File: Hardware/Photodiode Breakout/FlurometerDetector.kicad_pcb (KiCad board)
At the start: 2 copper layers, 25.4 x 25.4 mm, 6 parts, among them U1 OPA333xxDBV

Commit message: Breakout rearranging, LED wiring
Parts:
- moved C1 8.35 mm to (142.0, 70.4)
- moved U1 8.35 mm to (138.2, 67.8)
- moved C2 8.35 mm to (141.9, 68.5)
- moved D1 8.35 mm to (133.5, 68.9)
- moved R1 8.35 mm to (141.9, 66.5)
- moved Conn1 8.35 mm to (129.9, 62.1)
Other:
- board outline removed
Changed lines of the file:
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@@
   (net 4 "GND")
   (footprint "MRDT_Connectors:MOLEX_SL_03_Horizontal" (layer "F.Cu")
-    (at 135.89 67.945)
+    (at 129.921 62.103)
     (property "Sheetfile" "FlurometerDetector.kicad_sch")
     (property "Sheetname" "")
@@
   )
   (footprint "Package_TO_SOT_THT:TO-18-2" (layer "F.Cu")
-    (at 139.515276 74.745276 180)
+    (at 133.546276 68.903276 180)
     (descr "TO-18-2")
     (tags "TO-18-2")
@@
   )
   (footprint "Capacitor_SMD:C_0603_1608Metric_Pad1.08x0.95mm_HandSolder" (layer "F.Cu")
-    (at 147.955 76.2)
+    (at 141.986 70.358)
     (descr "Capacitor SMD 0603 (1608 Metric), square (rectangular) end terminal, IPC_7351 nominal with elongated pad for handsoldering. (Body size source: IPC-SM-782 page 76, https://www.pcb-3d.com/wordpress/wp-content/uploads/ipc-sm-782a_amendment_1_and_2.pdf), generated with kicad-footprint-generator")
     (tags "capacitor handsolder")
@@
   )
   (footprint "Resistor_SMD:R_0603_1608Metric_Pad0.98x0.95mm_HandSolder" (layer "F.Cu")
-    (at 147.918 72.39)
+    (at 141.949 66.548)
     (descr "Resistor SMD 0603 (1608 Metric), square (rectangular) end terminal, IPC_7351 nominal with elongated pad for handsoldering. (Body size source: IPC-SM-782 page 72, https://www.pcb-3d.com/wordpress/wp-content/uploads/ipc-sm-782a_amendment_1_and_2.pdf), generated with kicad-footprint-generator")
     (tags "resistor handsolder")
@@
   )
   (footprint "Package_TO_SOT_SMD:SOT-23-5" (layer "F.Cu")
-    (at 144.145 73.66 -90)
+    (at 138.176 67.818 -90)
     (descr "SOT, 5 Pin (https://www.jedec.org/sites/default/files/docs/Mo-178c.PDF variant AA), generated with kicad-footprint-generator ipc_gullwing_generator.py")
     (tags "SOT TO_SOT_SMD")
@@
   )
   (footprint "Capacitor_SMD:C_0603_1608Metric_Pad1.08x0.95mm_HandSolder" (layer "F.Cu")
-    (at 147.918 74.295)
+    (at 141.949 68.453)
     (descr "Capacitor SMD 0603 (1608 Metric), square (rectangular) end terminal, IPC_7351 nominal with elongated pad for handsoldering. (Body size source: IPC-SM-782 page 76, https://www.pcb-3d.com/wordpress/wp-content/uploads/ipc-sm-782a_amendment_1_and_2.pdf), generated with kicad-footprint-generator")
     (tags "capacitor handsolder")
@@
     )
   )
-  (gr_line (start 151.13 87.63) (end 125.73 87.63) (layer "Edge.Cuts") (width 0.1))
-  (gr_line (start 125.73 62.23) (end 151.13 62.23) (layer "Edge.Cuts") (width 0.1))
-  (gr_line (start 125.73 87.63) (end 125.73 62.23) (layer "Edge.Cuts") (width 0.1))
-  (gr_line (start 151.13 62.23) (end 151.13 87.63) (layer "Edge.Cuts") (width 0.1))
+  (dimension (type aligned) (layer "F.Fab")
+    (pts (xy 151.13 49.53) (xy 151.13 87.63))
+    (height -2.54)
+    (gr_text "1500.0000 mils" (at 152.52 68.58 90) (layer "F.Fab")
+      (effects (font (size 1 1) (thickness 0.15)))
+    )
+    (format (units 3) (units_format 1) (precision 4))
+    (style (thickness 0.1) (arrow_length 1.27) (text_position_mode 0) (extension_height 0.58642) (extension_offset 0.5) keep_text_aligned)
+  )
+  (dimension (type aligned) (layer "F.Fab")
+    (pts (xy 113.03 87.63) (xy 151.13 87.63))
+    (height 3.302)
+    (gr_text "1500.0000 mils" (at 132.08 89.782) (layer "F.Fab")
+      (effects (font (size 1 1) (thickness 0.15)))
+    )
+    (format (units 3) (units_format 1) (precision 4))
+    (style (thickness 0.1) (arrow_length 1.27) (text_position_mode 0) (extension_height 0.58642) (extension_offset 0.5) keep_text_aligned)
+  )
 )

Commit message: Breakout Boards
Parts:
- added V1: Via, MRDT_Drill_Holes:4_40_Hole, F.Cu at (147.1, 53.6)
- added V2: Via, MRDT_Drill_Holes:4_40_Hole, F.Cu at (117.1, 83.6)
- added V3: Via, MRDT_Drill_Holes:4_40_Hole, F.Cu at (117.1, 53.6)
- added V4: Via, MRDT_Drill_Holes:4_40_Hole, F.Cu at (147.1, 83.6)
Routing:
- net Net-(C1-Pad2): track 0.00 -> 15.1 mm
- net +5V: track 0.00 -> 12.0 mm
- net Net-(C1-Pad1): track 0.00 -> 12.0 mm
- added copper zone on F.Cu, net GND
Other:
- board outline added: 38.1 x 38.1 mm
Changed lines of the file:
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@@
   )
   (setup
+    (stackup
+      (layer "F.SilkS" (type "Top Silk Screen"))
+      (layer "F.Paste" (type "Top Solder Paste"))
+      (layer "F.Mask" (type "Top Solder Mask") (thickness 0.01))
+      (layer "F.Cu" (type "copper") (thickness 0.035))
+      (layer "dielectric 1" (type "core") (thickness 1.51) (material "FR4") (epsilon_r 4.5) (loss_tangent 0.02))
+      (layer "B.Cu" (type "copper") (thickness 0.035))
+      (layer "B.Mask" (type "Bottom Solder Mask") (thickness 0.01))
+      (layer "B.Paste" (type "Bottom Solder Paste"))
+      (layer "B.SilkS" (type "Bottom Silk Screen"))
+      (copper_finish "None")
+      (dielectric_constraints no)
+    )
     (pad_to_mask_clearance 0)
     (pcbplotparams
@@
     (property "Sheetname" "")
     (attr smd)
-    (fp_text reference "C1" (at 0 -1.43) (layer "F.SilkS")
+    (fp_text reference "C1" (at 2.54 0) (layer "F.SilkS")
       (effects (font (size 1 1) (thickness 0.15)))
     )
@@
     )
   )
+  (footprint "MRDT_Drill_Holes:4_40_Hole" (layer "F.Cu")
+    (at 117.094 83.566)
+    (property "Sheetfile" "FlurometerDetector.kicad_sch")
+    (property "Sheetname" "")
+    (clearance 2.54)
+    (attr through_hole)
+    (fp_text reference "V2" (at -0.00508 0.50508) (layer "F.SilkS") hide
+      (effects (font (size 1 1) (thickness 0.15)))
+    )
+    (fp_text value "Via" (at -0.00508 -0.49492) (layer "F.Fab") hide
+      (effects (font (size 1 1) (thickness 0.15)))
+    )
+    (fp_circle (center 0 0) (end -0.00508 4.01828) (layer "F.SilkS") (width 0.15) (fill none))
+    (pad "" np_thru_hole circle locked (at 0 0) (size 2.9464 2.9464) (drill 2.9464) (layers *.Cu *.Mask)
+      (clearance 2.5))
+  )
   (footprint "Resistor_SMD:R_0603_1608Metric_Pad0.98x0.95mm_HandSolder" (layer "F.Cu")
     (at 141.949 66.548)
@@
     (property "Sheetname" "")
     (attr smd)
-    (fp_text reference "R1" (at 0 -1.43) (layer "F.SilkS")
+    (fp_text reference "R1" (at 2.577 0) (layer "F.SilkS")
       (effects (font (size 1 1) (thickness 0.15)))
     )
@@
       (rotate (xyz 0 0 0))
     )
+  )
+  (footprint "MRDT_Drill_Holes:4_40_Hole" (layer "F.Cu")
+    (at 147.066 53.594)
+    (property "Sheetfile" "FlurometerDetector.kicad_sch")
+    (property "Sheetname" "")
+    (clearance 2.54)
+    (attr through_hole)
+    (fp_text reference "V1" (at -0.00508 0.50508) (layer "F.SilkS") hide
+      (effects (font (size 1 1) (thickness 0.15)))
+    )
+    (fp_text value "Via" (at -0.00508 -0.49492) (layer "F.Fab") hide
+      (effects (font (size 1 1) (thickness 0.15)))
+    )
+    (fp_circle (center 0 0) (end -0.00508 4.01828) (layer "F.SilkS") (width 0.15) (fill none))
+    (pad "" np_thru_hole circle locked (at 0 0) (size 2.9464 2.9464) (drill 2.9464) (layers *.Cu *.Mask)
+      (clearance 2.5))
   )
   (footprint "Package_TO_SOT_SMD:SOT-23-5" (layer "F.Cu")
@@
     (property "Sheetname" "")
     (attr smd)
-    (fp_text reference "C2" (at 0 -1.43) (layer "F.SilkS")
+    (fp_text reference "C2" (at 2.577 0.127) (layer "F.SilkS")
       (effects (font (size 1 1) (thickness 0.15)))
     )
@@
     )
   )
+  (footprint "MRDT_Drill_Holes:4_40_Hole" (layer "F.Cu")
+    (at 147.066 83.566)
+    (property "Sheetfile" "FlurometerDetector.kicad_sch")
+    (property "Sheetname" "")
+    (clearance 2.54)
+    (attr through_hole)
+    (fp_text reference "V4" (at -0.00508 0.50508) (layer "F.SilkS") hide
+      (effects (font (size 1 1) (thickness 0.15)))
+    )
+    (fp_text value "Via" (at -0.00508 -0.49492) (layer "F.Fab") hide
+      (effects (font (size 1 1) (thickness 0.15)))
+    )
+    (fp_circle (center 0 0) (end -0.00508 4.01828) (layer "F.SilkS") (width 0.15) (fill none))
+    (pad "" np_thru_hole circle locked (at 0 0) (size 2.9464 2.9464) (drill 2.9464) (layers *.Cu *.Mask)
+      (clearance 2.5))
+  )
+  (footprint "MRDT_Drill_Holes:4_40_Hole" (layer "F.Cu")
+    (at 117.094 53.594)
+    (property "Sheetfile" "FlurometerDetector.kicad_sch")
+    (property "Sheetname" "")
+    (clearance 2.54)
+    (attr through_hole)
+    (fp_text reference "V3" (at -0.00508 0.50508) (layer "F.SilkS") hide
+      (effects (font (size 1 1) (thickness 0.15)))
+    )
+    (fp_text value "Via" (at -0.00508 -0.49492) (layer "F.Fab") hide
+      (effects (font (size 1 1) (thickness 0.15)))
+    )
+    (fp_circle (center 0 0) (end -0.00508 4.01828) (layer "F.SilkS") (width 0.15) (fill none))
+    (pad "" np_thru_hole circle locked (at 0 0) (size 2.9464 2.9464) (drill 2.9464) (layers *.Cu *.Mask)
+      (clearance 2.5))
+  )
+  (gr_line (start 117.094 87.63) (end 147.066 87.63) (layer "Edge.Cuts") (width 0.1))
+  (gr_arc (start 117.094 87.63) (mid 114.220318 86.439682) (end 113.03 83.566) (layer "Edge.Cuts") (width 0.1))
+  (gr_line (start 151.13 83.566) (end 151.13 53.594) (layer "Edge.Cuts") (width 0.1))
+  (gr_line (start 113.03 53.594) (end 113.03 83.566) (layer "Edge.Cuts") (width 0.1))
+  (gr_line (start 147.066 49.53) (end 117.094 49.53) (layer "Edge.Cuts") (width 0.1))
+  (gr_arc (start 113.03 53.594) (mid 114.220318 50.720318) (end 117.094 49.53) (layer "Edge.Cuts") (width 0.1))
+  (gr_arc (start 151.13 83.566) (mid 149.939682 86.439682) (end 147.066 87.63) (layer "Edge.Cuts") (width 0.1))
+  (gr_arc (start 147.066 49.53) (mid 149.939682 50.720318) (end 151.13 53.594) (layer "Edge.Cuts") (width 0.1))
   (dimension (type aligned) (layer "F.Fab")
     (pts (xy 151.13 49.53) (xy 151.13 87.63))
@@
     (style (thickness 0.1) (arrow_length 1.27) (text_position_mode 0) (extension_height 0.58642) (extension_offset 0.5) keep_text_aligned)
   )
+  (segment (start 141.1235 70.358) (end 138.6285 70.358) (width 0.254) (layer "F.Cu") (net 1))
+  (segment (start 141.0365 66.548) (end 141.0365 68.6465) (width 0.254) (layer "F.Cu") (net 1))
+  (segment (start 141.0365 70.271) (end 141.1235 70.358) (width 0.254) (layer "F.Cu") (net 1))
+  (segment (start 137.173776 68.903276) (end 133.546276 68.903276) (width 0.254) (layer "F.Cu") (net 1))
+  (segment (start 138.6285 70.358) (end 137.226 68.9555) (width 0.254) (layer "F.Cu") (net 1))
+  (segment (start 137.226 68.9555) (end 137.173776 68.903276) (width 0.254) (layer "F.Cu") (net 1))
+  (segment (start 141.0365 68.6465) (end 141.0365 70.271) (width 0.254) (layer "F.Cu") (net 1))
+  (segment (start 142.8615 66.548) (end 141.7185 65.405) (width 0.254) (layer "F.Cu") (net 2))
+  (segment (start 139.126 66.228) (end 139.126 66.6805) (width 0.254) (layer "F.Cu") (net 2))
+  (segment (start 135.001 62.103) (end 138.303 65.405) (width 0.254) (layer "F.Cu") (net 2))
+  (segment (start 142.8615 66.548) (end 142.8615 70.345) (width 0.254) (layer "F.Cu") (net 2))
+  (segment (start 141.7185 65.405) (end 138.303 65.405) (width 0.254) (layer "F.Cu") (net 2))
+  (segment (start 142.8615 70.345) (end 142.8485 70.358) (width 0.254) (layer "F.Cu") (net 2))
+  (segment (start 138.303 65.405) (end 139.126 66.228) (width 0.254) (layer "F.Cu") (net 2))
+  (segment (start 135.7205 67.9025) (end 138.073 67.9025) (width 0.381) (layer "F.Cu") (net 3))
+  (segment (start 138.073 67.9025) (end 139.126 68.9555) (width 0.381) (layer "F.Cu") (net 3))
+  (segment (start 129.921 62.103) (end 135.7205 67.9025) (width 0.381) (layer "F.Cu") (net 3))
+  (zone (net 4) (net_name "GND") (layer "F.Cu") (hatch edge 0.508)
+    (connect_pads yes (clearance 0.508))
+    (min_thickness 0.254) (filled_areas_thickness no)
+    (fill yes (thermal_gap 0.508) (thermal_bridge_width 0.508))
+    (polygon
+      (pts
+        (xy 151.13 87.63)
+        (xy 113.03 87.63)
+        (xy 113.03 49.53)
+        (xy 151.13 49.53)
+      )
+    )
+  )
 )

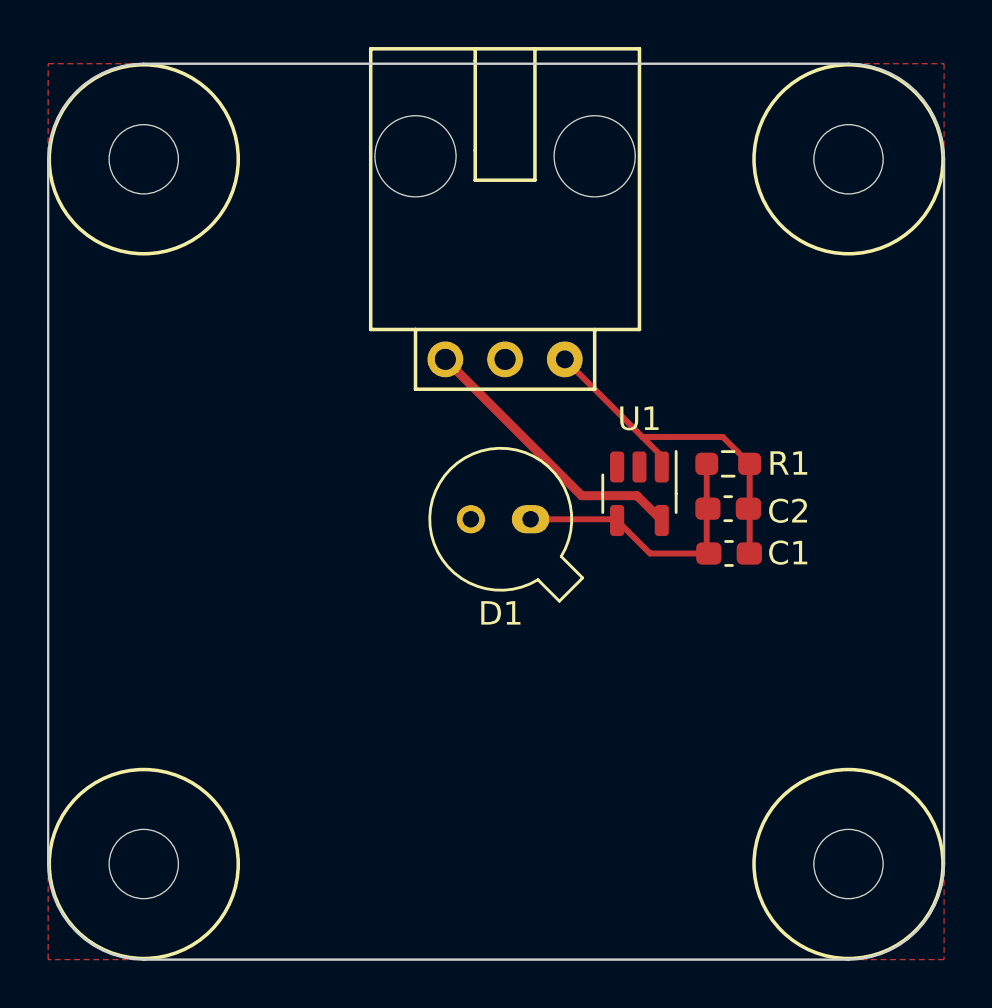
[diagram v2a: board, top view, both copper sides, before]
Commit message: Photodiode wire connections and labeling.
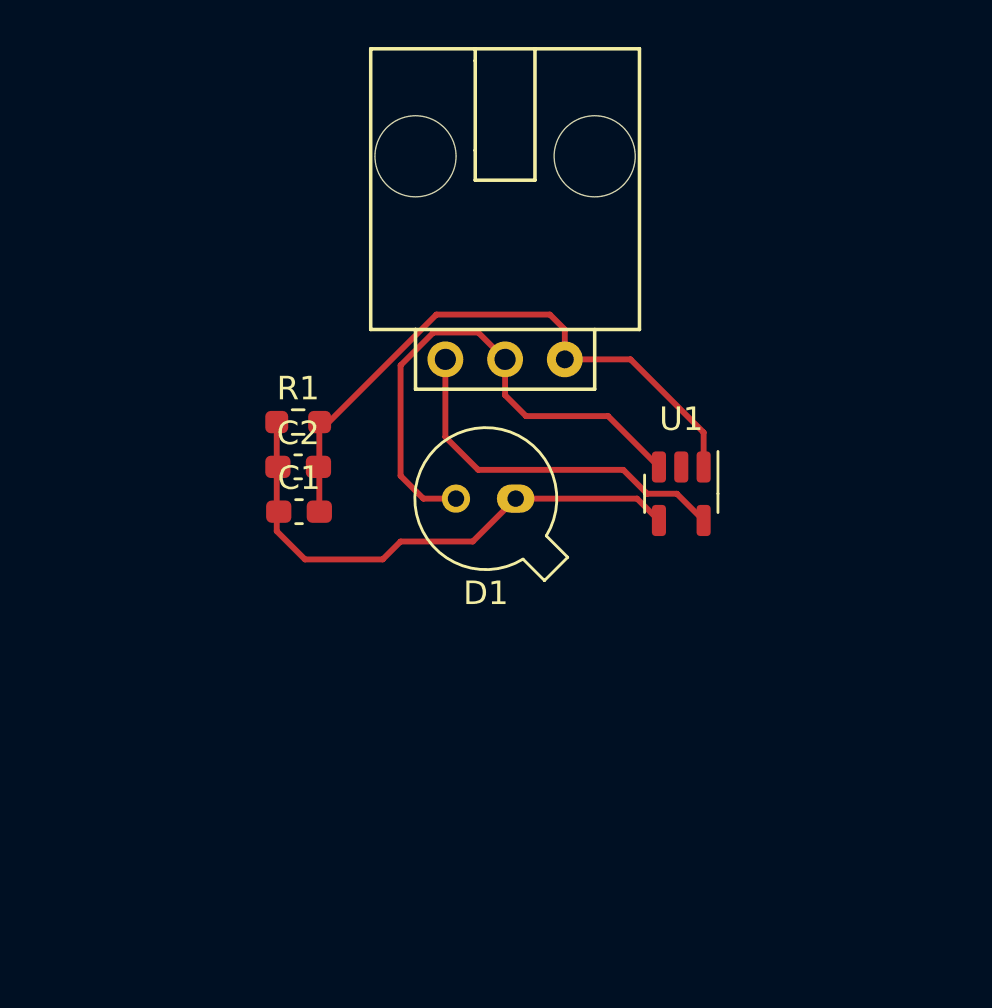
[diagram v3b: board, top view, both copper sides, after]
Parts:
- removed V1, V2, V3, V4: Via, MRDT_Drill_Holes:4_40_Hole
- moved C2 18.4 mm to (123.7, 66.7)
- moved R1 18.4 mm to (123.7, 64.8)
- moved C1 18.4 mm to (123.7, 68.6)
- moved U1 1.78 mm to (140.0, 67.8)
- moved D1 1.08 mm to (132.9, 68.0)
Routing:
- net GND: track 0.00 -> 22.3 mm
- net Net-(C1-Pad2): track 15.1 -> 26.1 mm
- net Net-(C1-Pad1): track 12.0 -> 22.8 mm
- net +5V: track 12.0 -> 15.8 mm
- removed copper zone on F.Cu, net GND
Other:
- board outline removed

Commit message: Revert "Photodiode wire connections and labeling."
This reverts commit 414c0e9564a782f982e7044c884eaa931a5570fb.
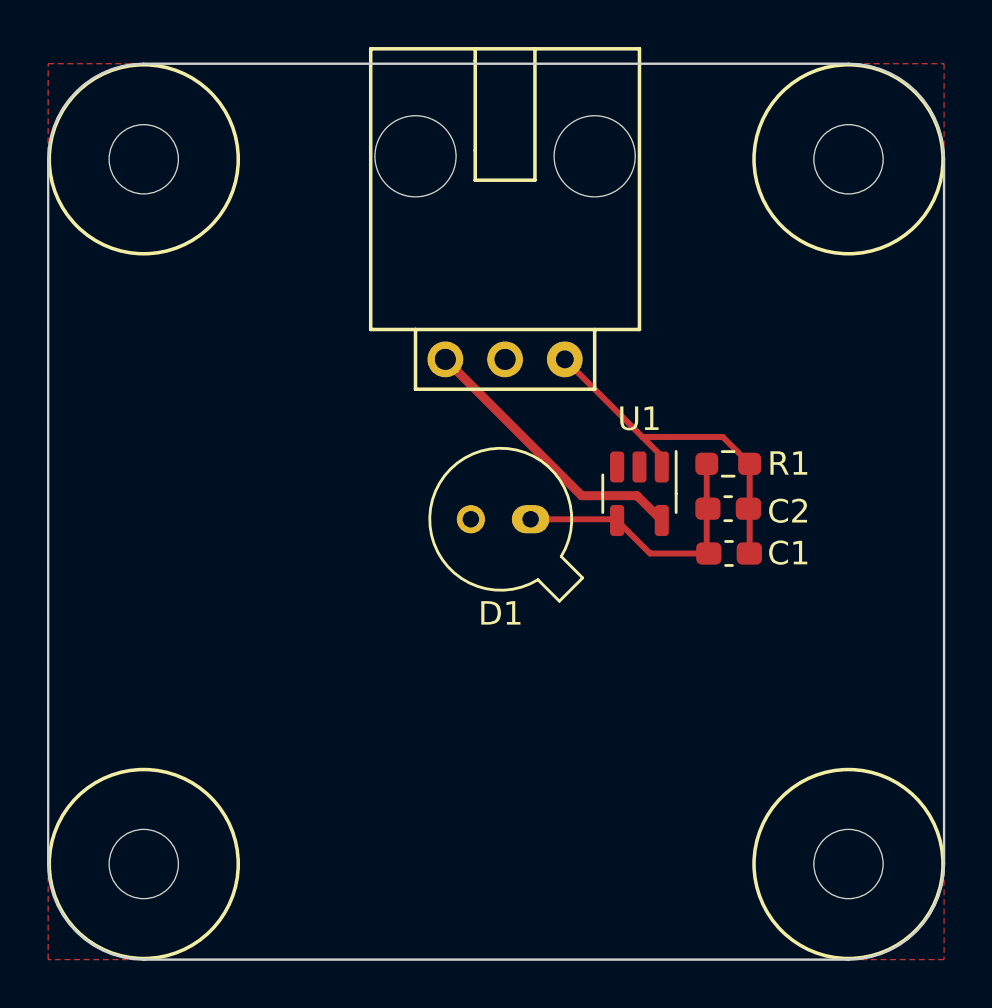
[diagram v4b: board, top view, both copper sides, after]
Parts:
- added V1: Via, MRDT_Drill_Holes:4_40_Hole, F.Cu at (147.1, 53.6)
- added V2: Via, MRDT_Drill_Holes:4_40_Hole, F.Cu at (117.1, 83.6)
- added V3: Via, MRDT_Drill_Holes:4_40_Hole, F.Cu at (117.1, 53.6)
- added V4: Via, MRDT_Drill_Holes:4_40_Hole, F.Cu at (147.1, 83.6)
- moved C2 18.4 mm to (141.9, 68.5)
- moved R1 18.4 mm to (141.9, 66.5)
- moved C1 18.4 mm to (142.0, 70.4)
- moved U1 1.78 mm to (138.2, 67.8)
- moved D1 1.08 mm to (133.5, 68.9)
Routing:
- net GND: track 22.3 -> 0.00 mm
- net Net-(C1-Pad2): track 26.1 -> 15.1 mm
- net Net-(C1-Pad1): track 22.8 -> 12.0 mm
- net +5V: track 15.8 -> 12.0 mm
- added copper zone on F.Cu, net GND
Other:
- board outline added: 38.1 x 38.1 mm
